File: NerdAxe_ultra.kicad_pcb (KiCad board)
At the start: 4 copper layers, 61.1 x 99.8 mm, 111 parts, among them J1 54-00164, J4 Conn_01x04, Q1 CSD17311Q5, Q2 CSD17311Q5, Q3 2N7002K, U1 25MHz, U10 DS4432U+, U14 BM1366_mode0, U2 TXB0104RGYR, U3 T-Display-S3, U5 MCP1824T-1802E, U6 MCP1824T-0802E, U7 EMC2101, U8 INA260, U9 TPS40305

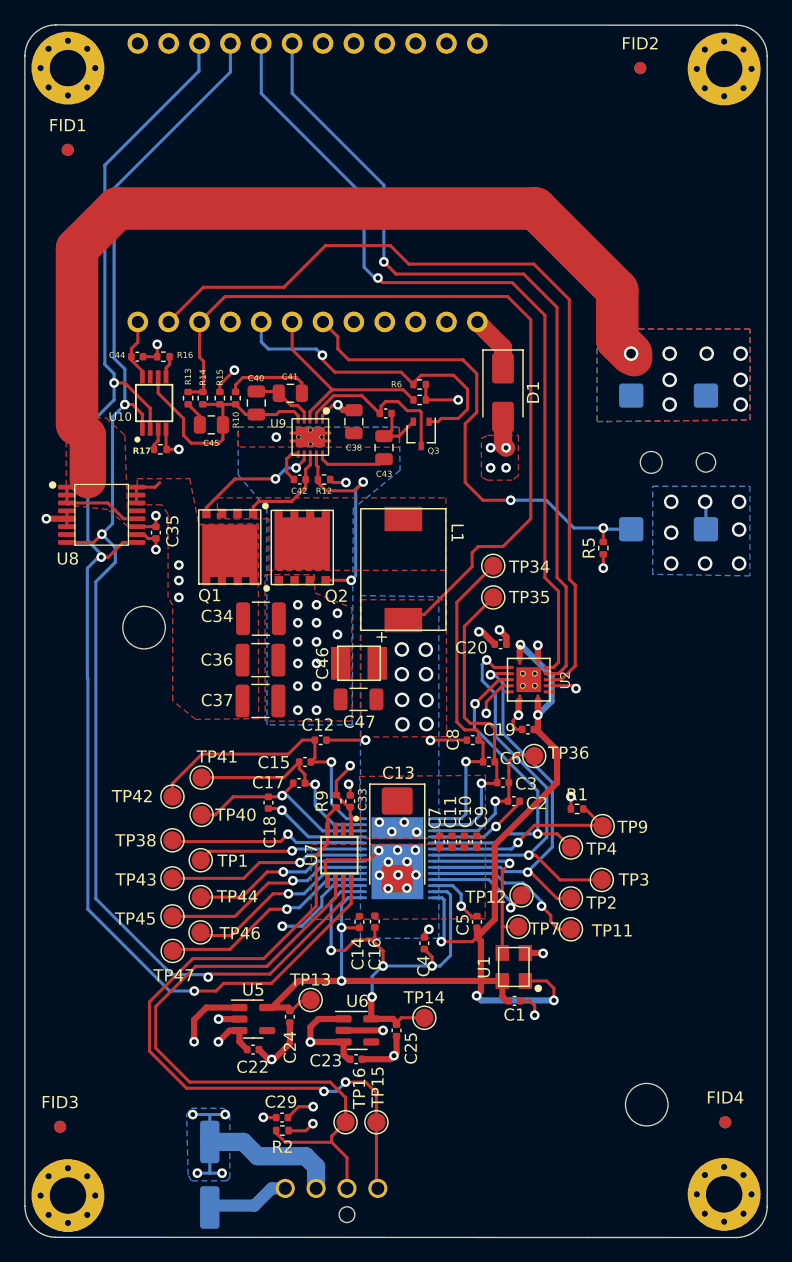
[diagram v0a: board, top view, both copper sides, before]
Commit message: NerdAxe 102
- Changed fan dissipator holes
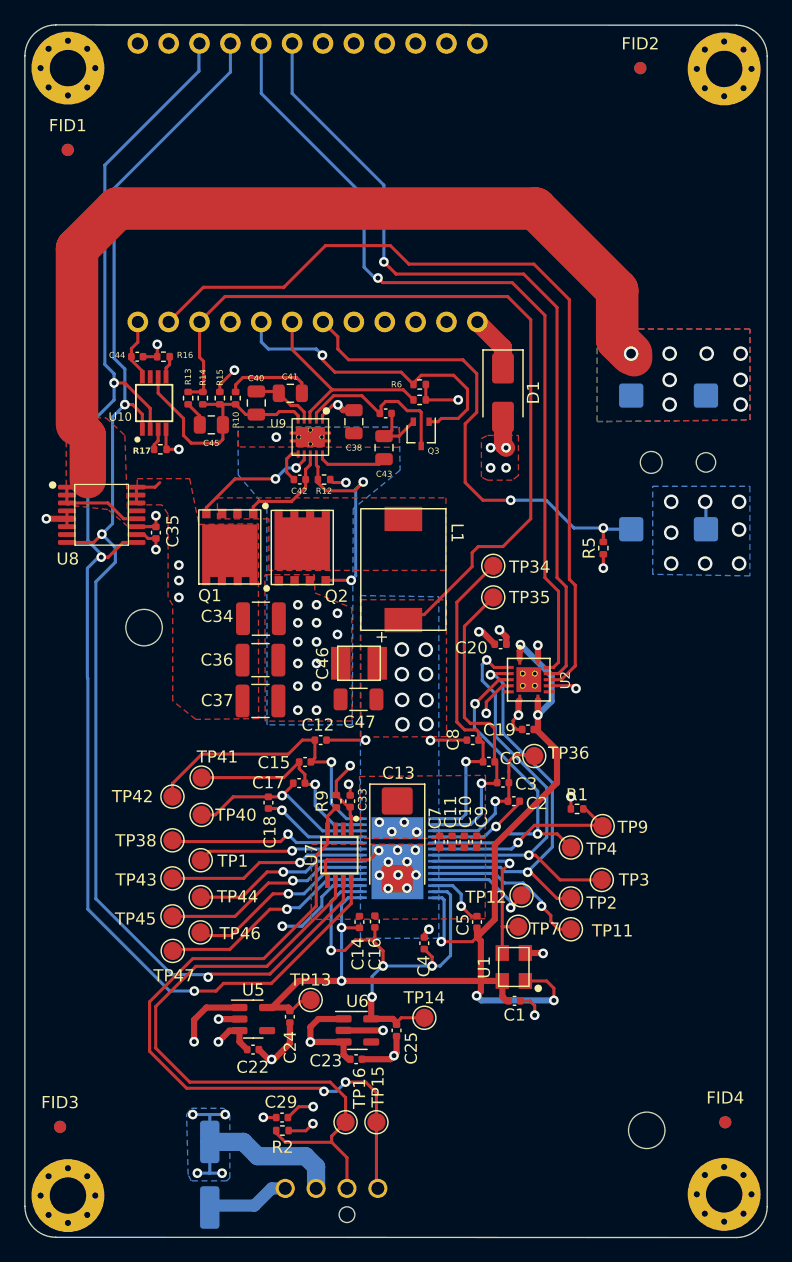
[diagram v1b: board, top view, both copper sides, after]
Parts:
- moved H5 0.98 mm to (126.4, 137.3)
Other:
- board text added: "BM1366 NERDAXE V1.0.2"
- board text removed: "BM1366 NERDAXE V1.0.1"
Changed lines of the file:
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@@
     (fp_circle (center 0 0) (end 3.75 0)
       (stroke (width 0.05) (type solid)) (fill none) (layer "F.CrtYd"))
-    (pad "" np_thru_hole circle (at 0 0) (size 3.5 3.5) (drill 3.5) (layers "F&B.Cu" "*.Mask"))
+    (pad "" np_thru_hole circle (at 0 0) (size 3 3) (drill 3) (layers "F&B.Cu" "*.Mask"))
   )
   (footprint "Capacitor_SMD:C_0805_2012Metric" (layer "F.Cu")
@@
   )
   (footprint "MountingHole:MountingHole_3.5mm" (layer "F.Cu")
-    (at 126.06 136.36)
+    (at 126.365 137.287)
     (descr "Mounting Hole 3.5mm, no annular")
     (tags "mounting hole 3.5mm no annular")
@@
     (fp_circle (center 0 0) (end 3.75 0)
       (stroke (width 0.05) (type solid)) (fill none) (layer "F.CrtYd"))
-    (pad "" np_thru_hole circle (at 0.07 -0.01) (size 3.5 3.5) (drill 3.5) (layers "F&B.Cu" "*.Mask"))
+    (pad "" np_thru_hole circle (at -0.235 1.174) (size 3 3) (drill 3) (layers "F&B.Cu" "*.Mask"))
   )
   (footprint "Capacitor_SMD:C_0402_1005Metric" (layer "F.Cu")
@@
       (solder_mask_margin 0.5) (clearance 0.5))
   )
+  (gr_rect (start 85.344 97.536) (end 125.603 137.668)
+    (stroke (width 0.15) (type default)) (fill none) (layer "Dwgs.User"))
   (gr_line (start 77.5 47.5) (end 133.5 47.522)
     (stroke (width 0.1) (type default)) (layer "Edge.Cuts"))
@@
     )
   )
-  (gr_text "BM1366 NERDAXE V1.0.1" (at 113.792 94.488) (layer "B.SilkS")
+  (gr_text "BM1366 NERDAXE V1.0.2" (at 113.792 94.488) (layer "B.SilkS")
     (effects (font (size 1 1) (thickness 0.15)) (justify mirror))
   )
